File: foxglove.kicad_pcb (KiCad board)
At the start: 4 copper layers, 70.7 x 53.3 mm, 168 parts, among them IC1 LFE5U-12F-6BG256C, J1 NEIGHBOR1, J2 NEIGHBOR2, J3 Conn_02x05_Odd_Even, J4 Conn_02x10_Odd_Even, J5 Conn_01x02_Female, J6 Conn_02x03_Odd_Even, J7 BONUS_ROW, U1 LM393, U10 SHIFTER, U11 74HC4051, U12 SHIFTER, U13 74HC4051, U14 SHIFTER, U15 74HC4051, U16 SHIFTER, U17 74HC4051, U18 SHIFTER, U19 74HC4051, U2 ADP225, U20 SHIFTER, U21 74HC4051, U22 SHIFTER, U23 74HC4051, U24 SHIFTER, U25 74LVC1G53, U26 PCA6408A, U3 AP2127, U4 74LVC1G3157, U5 AP2127, U6 AP2127, U7 DAC084S085, U8 AT25xxx, U9 74HC4051

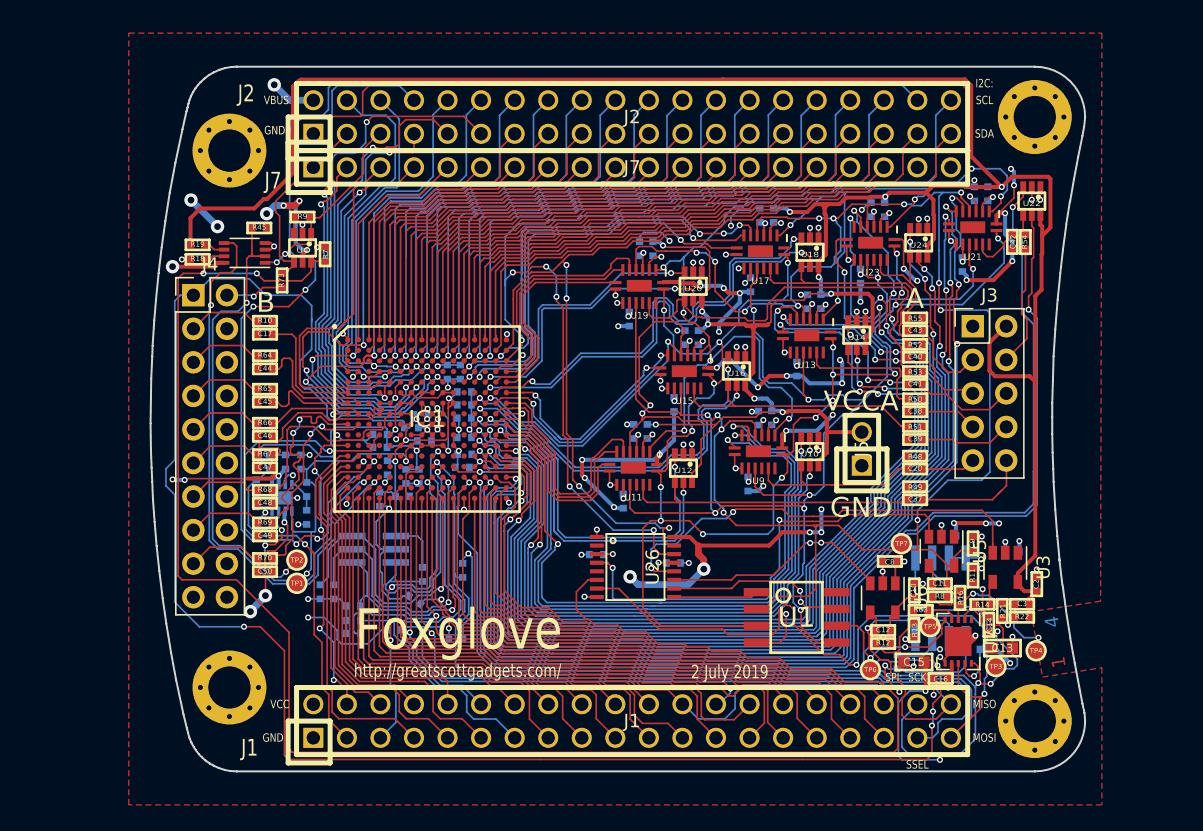
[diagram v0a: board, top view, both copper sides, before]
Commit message: Added silkscreen tables for banks and completed BOM data
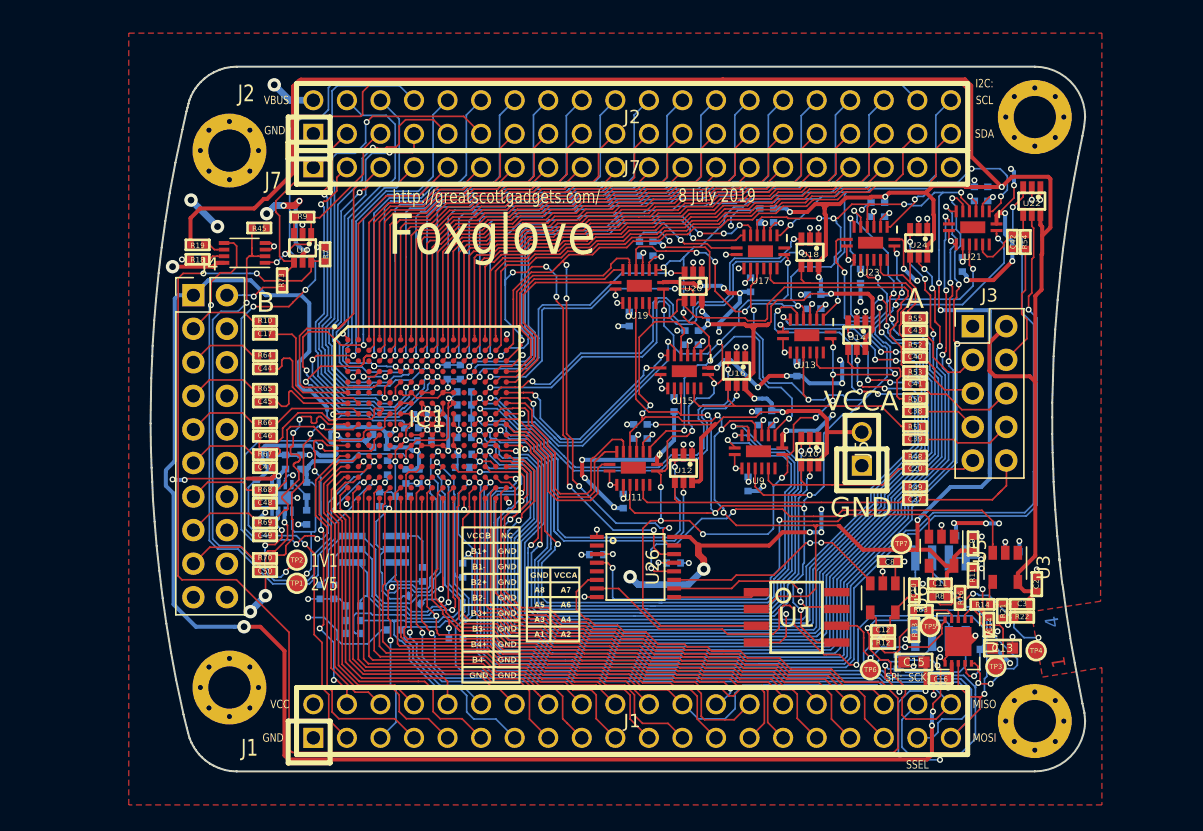
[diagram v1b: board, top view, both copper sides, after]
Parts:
- added G***: LOGO, gsg-modules:foxglove_bankB, F.Cu at (135.4, 109.3)
- added G***: LOGO, gsg-modules:foxglove_bankA, F.Cu at (140.1, 109.3)
- added G***: LOGO, gsg-modules:foxglove_jtag, B.Cu at (133.5, 102.9)
- turned R17 to 270 degrees
- turned R18 to 0 degrees
- turned R19 to 0 degrees
- turned R20 to 270 degrees
- turned R23 to 270 degrees
- turned R26 to 270 degrees
- turned R29 to 270 degrees
- turned R32 to 270 degrees
- turned R35 to 270 degrees
- turned R38 to 270 degrees
- turned R45 to 0 degrees
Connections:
- R17 pad 1: +5V -> /~E~_1
- R17 pad 2: /~E~_1 -> +5V
- R18 pad 1: Net-(R18-Pad1) -> GND
- R18 pad 2: GND -> Net-(R18-Pad2)
- R19 pad 1: Net-(R19-Pad1) -> /VCCA
- R19 pad 2: /VCCA -> Net-(R19-Pad2)
- R20 pad 1: +5V -> /~E~_2
- R20 pad 2: /~E~_2 -> +5V
- R23 pad 1: +5V -> /~E~_3
- R23 pad 2: /~E~_3 -> +5V
- R26 pad 1: +5V -> /~E~_4
- R26 pad 2: /~E~_4 -> +5V
- R29 pad 1: +5V -> /~E~_5
- R29 pad 2: /~E~_5 -> +5V
- R32 pad 1: +5V -> /~E~_6
- R32 pad 2: /~E~_6 -> +5V
- R35 pad 1: +5V -> /~E~_7
- R35 pad 2: /~E~_7 -> +5V
- R38 pad 1: +5V -> /~E~_8
- R38 pad 2: /~E~_8 -> +5V
- R45 pad 1: +5V -> /pull_en
- R45 pad 2: /pull_en -> +5V
- U25 pad 6: Net-(R19-Pad1) -> Net-(R19-Pad2)
- U25 pad 7: Net-(R18-Pad1) -> Net-(R18-Pad2)
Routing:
- net /DAC: track 153.9 -> 168.9 mm
- net GND: track 124.2 -> 127.8 mm
- net +1V1: track 47.5 -> 50.0 mm
- net +2V5: track 31.8 -> 34.3 mm
- net /VCCA: track 263.0 -> 264.9 mm
- net Net-(R19-Pad2): track 0.00 -> 1.62 mm
- net Net-(R19-Pad1): track 1.62 -> 0.00 mm
- net Net-(R18-Pad2): track 0.00 -> 1.57 mm
- net Net-(R18-Pad1): track 1.57 -> 0.00 mm
- net /J1.04: track 23.0 -> 24.1 mm
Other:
- board text added: "1V1"
- board text added: "2V5"
- board text added: "8 July 2019"
- board text added: "SPI FLASH"
- board text removed: "2 July 2019"

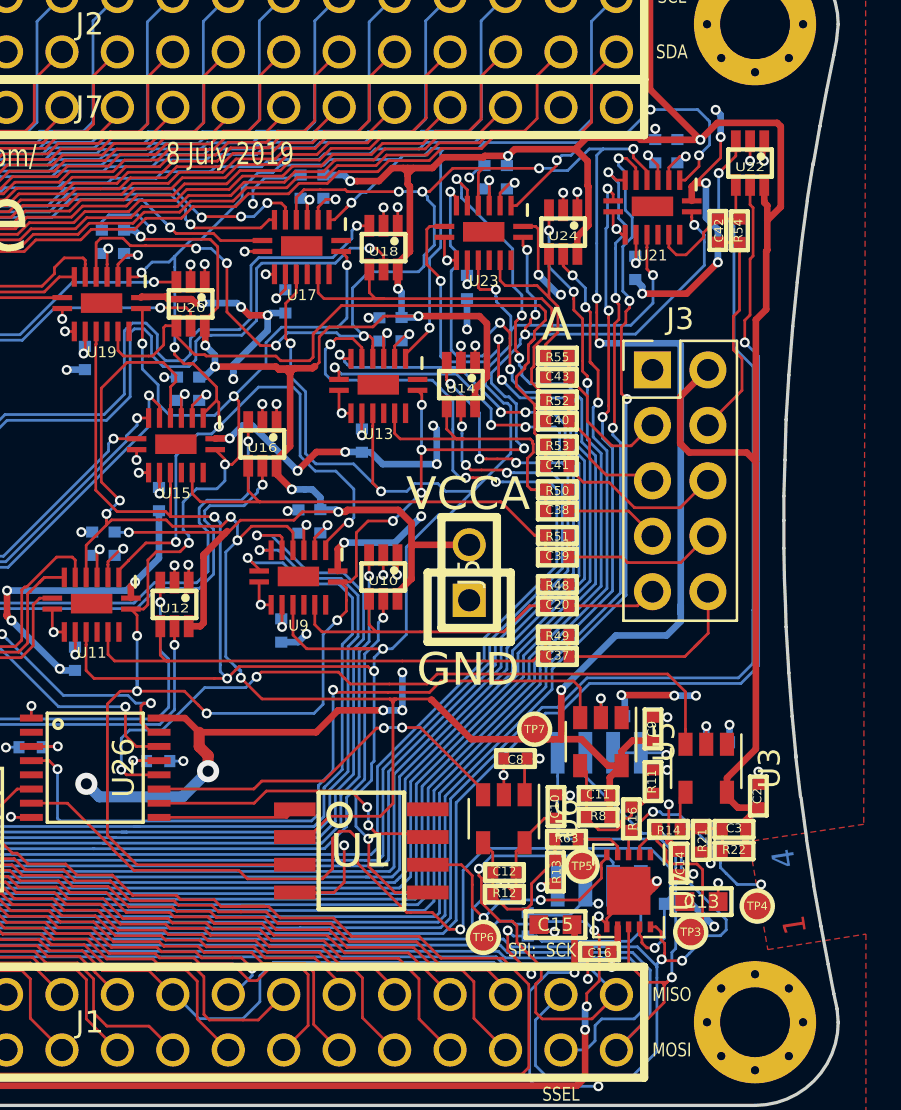
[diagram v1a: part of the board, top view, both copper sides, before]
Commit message: Corrected FPGA footprint
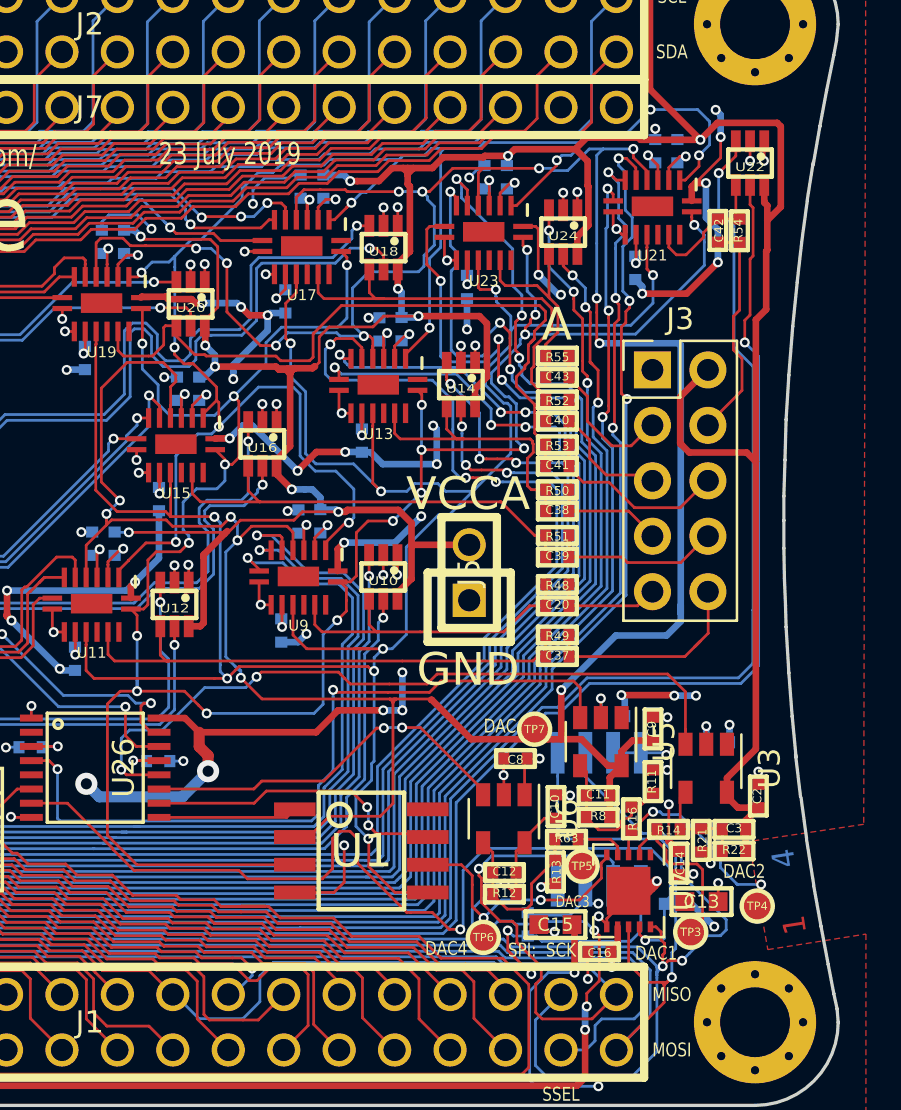
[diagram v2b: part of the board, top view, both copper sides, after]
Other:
- board text added: "23 July 2019"
- board text added: "DAC"
- board text added: "DAC1"
- board text added: "DAC2"
- board text added: "DAC3"
- board text added: "DAC4"
- board text removed: "8 July 2019"

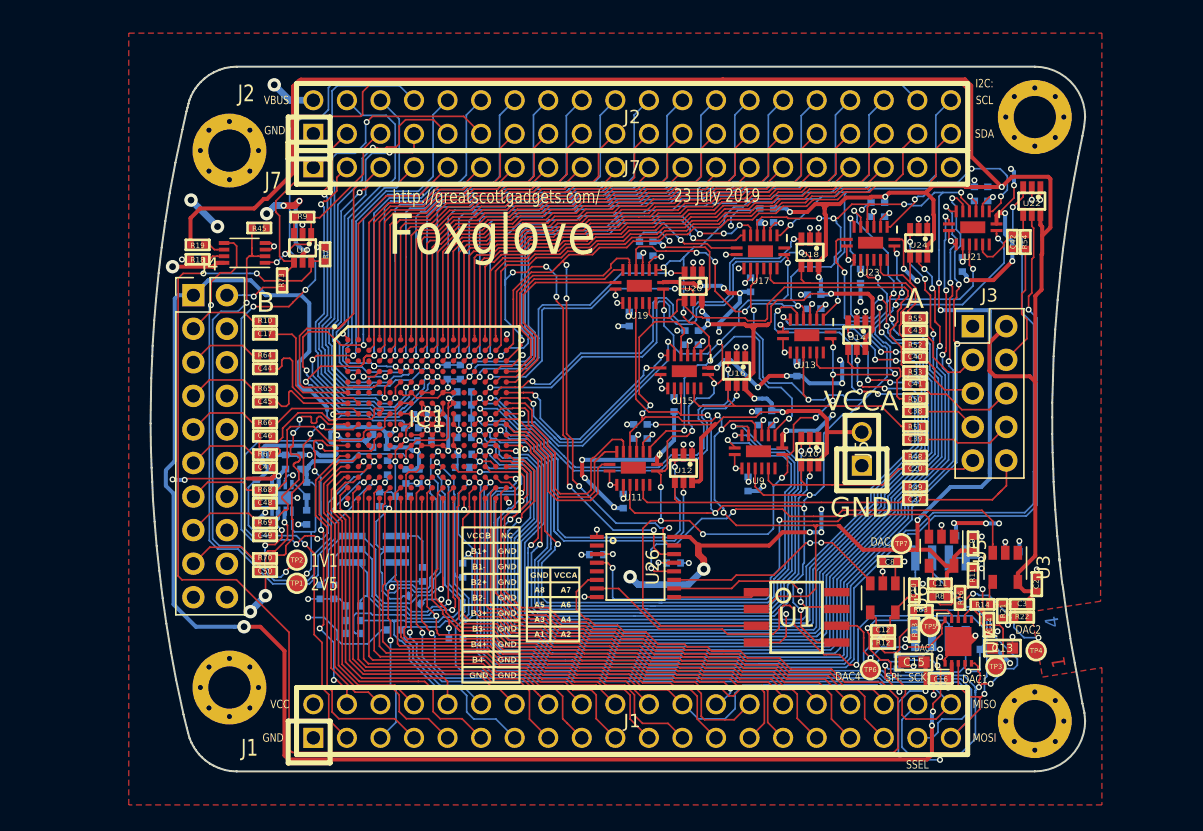
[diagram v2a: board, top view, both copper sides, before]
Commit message: Improved silkscreen table visibility and changed board edge cuts to support right-angle connectors
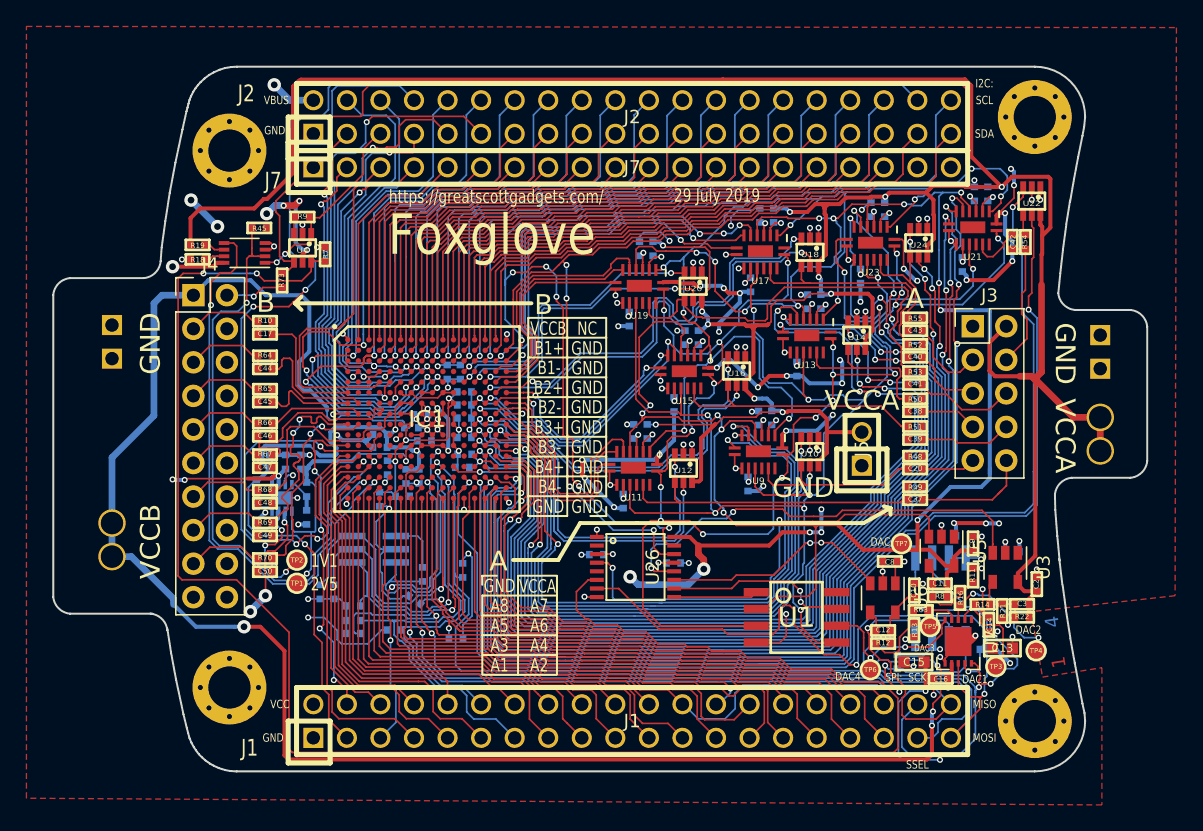
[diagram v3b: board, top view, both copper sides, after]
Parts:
- removed the G*** at (135.4, 109.3)
- removed the G*** at (140.1, 109.3)
- added TP10: TestPoint, gsg-modules:HEADER-1x1, B.Cu at (181.5, 91.4)
- added TP11: TestPoint, gsg-modules:HEADER-1x1-TESTPROBE, B.Cu at (181.5, 97.7)
- added TP12: TestPoint, gsg-modules:HEADER-1x1, B.Cu at (106.7, 90.7)
- added TP13: TestPoint, gsg-modules:HEADER-1x1-TESTPROBE, B.Cu at (106.7, 103.1)
- added TP14: TestPoint, gsg-modules:HEADER-1x1, B.Cu at (106.7, 88.1)
- added TP15: TestPoint, gsg-modules:HEADER-1x1-TESTPROBE, B.Cu at (106.7, 105.7)
- added TP8: TestPoint, gsg-modules:HEADER-1x1, B.Cu at (181.5, 88.9)
- added TP9: TestPoint, gsg-modules:HEADER-1x1-TESTPROBE, B.Cu at (181.5, 95.1)
- C18, C19, C23, C24, C25, C29, C30, C33, C34: value 100nF -> 0.1uF
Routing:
- net /VCCA: track 264.9 -> 274.6 mm
- net /VCCB: track 143.3 -> 148.2 mm
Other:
- board size 70.7 x 53.3 mm -> 82.8 x 53.3 mm
- board text added: "29 July 2019"
- board text added: "A1"
- board text added: "A2"
- board text added: "A3"
- board text added: "A4"
- board text added: "A5"
- board text added: "A6"
- board text added: "A7"
- board text added: "A8"
- board text added: "B1+"
- board text added: "B1-"
- board text added: "B2+"
- board text added: "B2-"
- board text added: "B3+"
- board text added: "B3-"
- board text added: "B4+"
- board text added: "B4-"
- board text added: "NC"
- board text added: "VCCB"
- board text added: "https://greatscottgadgets.com/"
- board text removed: "23 July 2019"
- board text removed: "http://greatscottgadgets.com/"

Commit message: Flipped J4 footprint
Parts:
- moved J4 23.1 mm to (115.4, 108.8), turned to 180 degrees
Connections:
- J4 pad 1: /VCCB -> GND
- J4 pad 10: GND -> /B3T_P
- J4 pad 11: /B3T_P -> GND
- J4 pad 12: GND -> /B2T_N
- J4 pad 13: /B3T_N -> GND
- J4 pad 14: GND -> /B2T_P
- J4 pad 15: /B4T_P -> GND
- J4 pad 16: GND -> /B1T_N
- J4 pad 17: /B4T_N -> GND
- J4 pad 18: GND -> /B1T_P
- J4 pad 19: GND -> /Vtarget
- J4 pad 2: /Vtarget -> GND
- J4 pad 20: GND -> /VCCB
- J4 pad 3: /B1T_P -> GND
- J4 pad 4: GND -> /B4T_N
- J4 pad 5: /B1T_N -> GND
- J4 pad 6: GND -> /B4T_P
- J4 pad 7: /B2T_P -> GND
- J4 pad 8: GND -> /B3T_N
- J4 pad 9: /B2T_N -> GND
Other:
- board text added: "13 August 2019"
- board text removed: "29 July 2019"
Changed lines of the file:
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@@
   )
   (setup
-    (last_trace_width 0.508)
+    (last_trace_width 0.127)
     (user_trace_width 0.127)
     (user_trace_width 0.3048)
@@
   )
   (module Connector_PinHeader_2.54mm:PinHeader_2x10_P2.54mm_Vertical (layer F.Cu)
-    (at 112.8395 85.8774)
+    (at 115.3922 108.7882 180)
     (descr "Through hole straight pin header, 2x10, 2.54mm pitch, double rows")
     (tags "Through hole pin header THT 2x10 2.54mm double row")
-    (fp_text reference J4 (at 1.27 -2.33) (layer F.SilkS)
+    (fp_text reference J4 (at 1.27 -2.33 180) (layer F.SilkS)
       (effects (font (size 1 1) (thickness 0.15)))
     )
-    (fp_text value Conn_02x10_Odd_Even (at 1.27 25.19) (layer F.Fab)
+    (fp_text value Conn_02x10_Odd_Even (at 1.27 25.19 180) (layer F.Fab)
       (effects (font (size 1 1) (thickness 0.15)))
     )
@@
     (fp_line (start 4.35 24.65) (end 4.35 -1.8) (layer F.CrtYd) (width 0.05))
     (fp_line (start 4.35 -1.8) (end -1.8 -1.8) (layer F.CrtYd) (width 0.05))
-    (fp_text user %R (at 1.27 11.43 90) (layer F.Fab)
+    (fp_text user %R (at 1.27 11.43 270) (layer F.Fab)
       (effects (font (size 1 1) (thickness 0.15)))
     )
-    (pad 1 thru_hole rect (at 0 0) (size 1.7 1.7) (drill 1) (layers *.Cu *.Mask)
-      (net 122 /VCCB))
-    (pad 2 thru_hole oval (at 2.54 0) (size 1.7 1.7) (drill 1) (layers *.Cu *.Mask)
-      (net 305 /Vtarget))
-    (pad 3 thru_hole oval (at 0 2.54) (size 1.7 1.7) (drill 1) (layers *.Cu *.Mask)
-      (net 297 /B1T_P))
-    (pad 4 thru_hole oval (at 2.54 2.54) (size 1.7 1.7) (drill 1) (layers *.Cu *.Mask)
+    (pad 1 thru_hole rect (at 0 0 180) (size 1.7 1.7) (drill 1) (layers *.Cu *.Mask)
       (net 1 GND))
-    (pad 5 thru_hole oval (at 0 5.08) (size 1.7 1.7) (drill 1) (layers *.Cu *.Mask)
-      (net 298 /B1T_N))
-    (pad 6 thru_hole oval (at 2.54 5.08) (size 1.7 1.7) (drill 1) (layers *.Cu *.Mask)
+    (pad 2 thru_hole oval (at 2.54 0 180) (size 1.7 1.7) (drill 1) (layers *.Cu *.Mask)
       (net 1 GND))
-    (pad 7 thru_hole oval (at 0 7.62) (size 1.7 1.7) (drill 1) (layers *.Cu *.Mask)
-      (net 299 /B2T_P))
-    (pad 8 thru_hole oval (at 2.54 7.62) (size 1.7 1.7) (drill 1) (layers *.Cu *.Mask)
+    (pad 3 thru_hole oval (at 0 2.54 180) (size 1.7 1.7) (drill 1) (layers *.Cu *.Mask)
       (net 1 GND))
-    (pad 9 thru_hole oval (at 0 10.16) (size 1.7 1.7) (drill 1) (layers *.Cu *.Mask)
-      (net 300 /B2T_N))
-    (pad 10 thru_hole oval (at 2.54 10.16) (size 1.7 1.7) (drill 1) (layers *.Cu *.Mask)
+    (pad 4 thru_hole oval (at 2.54 2.54 180) (size 1.7 1.7) (drill 1) (layers *.Cu *.Mask)
+      (net 304 /B4T_N))
+    (pad 5 thru_hole oval (at 0 5.08 180) (size 1.7 1.7) (drill 1) (layers *.Cu *.Mask)
       (net 1 GND))
-    (pad 11 thru_hole oval (at 0 12.7) (size 1.7 1.7) (drill 1) (layers *.Cu *.Mask)
-      (net 301 /B3T_P))
-    (pad 12 thru_hole oval (at 2.54 12.7) (size 1.7 1.7) (drill 1) (layers *.Cu *.Mask)
+    (pad 6 thru_hole oval (at 2.54 5.08 180) (size 1.7 1.7) (drill 1) (layers *.Cu *.Mask)
+      (net 303 /B4T_P))
+    (pad 7 thru_hole oval (at 0 7.62 180) (size 1.7 1.7) (drill 1) (layers *.Cu *.Mask)
       (net 1 GND))
-    (pad 13 thru_hole oval (at 0 15.24) (size 1.7 1.7) (drill 1) (layers *.Cu *.Mask)
+    (pad 8 thru_hole oval (at 2.54 7.62 180) (size 1.7 1.7) (drill 1) (layers *.Cu *.Mask)
       (net 302 /B3T_N))
-    (pad 14 thru_hole oval (at 2.54 15.24) (size 1.7 1.7) (drill 1) (layers *.Cu *.Mask)
+    (pad 9 thru_hole oval (at 0 10.16 180) (size 1.7 1.7) (drill 1) (layers *.Cu *.Mask)
       (net 1 GND))
-    (pad 15 thru_hole oval (at 0 17.78) (size 1.7 1.7) (drill 1) (layers *.Cu *.Mask)
-      (net 303 /B4T_P))
-    (pad 16 thru_hole oval (at 2.54 17.78) (size 1.7 1.7) (drill 1) (layers *.Cu *.Mask)
+    (pad 10 thru_hole oval (at 2.54 10.16 180) (size 1.7 1.7) (drill 1) (layers *.Cu *.Mask)
+      (net 301 /B3T_P))
+    (pad 11 thru_hole oval (at 0 12.7 180) (size 1.7 1.7) (drill 1) (layers *.Cu *.Mask)
       (net 1 GND))
-    (pad 17 thru_hole oval (at 0 20.32) (size 1.7 1.7) (drill 1) (layers *.Cu *.Mask)
-      (net 304 /B4T_N))
-    (pad 18 thru_hole oval (at 2.54 20.32) (size 1.7 1.7) (drill 1) (layers *.Cu *.Mask)
+    (pad 12 thru_hole oval (at 2.54 12.7 180) (size 1.7 1.7) (drill 1) (layers *.Cu *.Mask)
+      (net 300 /B2T_N))
+    (pad 13 thru_hole oval (at 0 15.24 180) (size 1.7 1.7) (drill 1) (layers *.Cu *.Mask)
       (net 1 GND))
-    (pad 19 thru_hole oval (at 0 22.86) (size 1.7 1.7) (drill 1) (layers *.Cu *.Mask)
+    (pad 14 thru_hole oval (at 2.54 15.24 180) (size 1.7 1.7) (drill 1) (layers *.Cu *.Mask)
+      (net 299 /B2T_P))
+    (pad 15 thru_hole oval (at 0 17.78 180) (size 1.7 1.7) (drill 1) (layers *.Cu *.Mask)
       (net 1 GND))
-    (pad 20 thru_hole oval (at 2.54 22.86) (size 1.7 1.7) (drill 1) (layers *.Cu *.Mask)
+    (pad 16 thru_hole oval (at 2.54 17.78 180) (size 1.7 1.7) (drill 1) (layers *.Cu *.Mask)
+      (net 298 /B1T_N))
+    (pad 17 thru_hole oval (at 0 20.32 180) (size 1.7 1.7) (drill 1) (layers *.Cu *.Mask)
       (net 1 GND))
+    (pad 18 thru_hole oval (at 2.54 20.32 180) (size 1.7 1.7) (drill 1) (layers *.Cu *.Mask)
+      (net 297 /B1T_P))
+    (pad 19 thru_hole oval (at 0 22.86 180) (size 1.7 1.7) (drill 1) (layers *.Cu *.Mask)
+      (net 305 /Vtarget))
+    (pad 20 thru_hole oval (at 2.54 22.86 180) (size 1.7 1.7) (drill 1) (layers *.Cu *.Mask)
+      (net 122 /VCCB))
     (model ${KISYS3DMOD}/Connector_PinHeader_2.54mm.3dshapes/PinHeader_2x10_P2.54mm_Vertical.wrl
       (at (xyz 0 0 0))
@@
     (effects (font (size 1.5 1.5) (thickness 0.3)))
   )
-  (gr_text "29 July 2019" (at 152.4762 78.3336) (layer F.SilkS)
+  (gr_text "13 August 2019" (at 152.4762 78.3336) (layer F.SilkS)
     (effects (font (size 1.016 0.762) (thickness 0.1524)))
   )
